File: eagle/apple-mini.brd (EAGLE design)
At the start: 127 x 73.7 mm, 41 parts, among them J1 USBMICRO, J2 JTAG, J3 RBM22DRTN, U1 FT240XS, U2 SN74LVC2G17DBV, U3 TPS2082D, U4 MCS6502, U5 MC6821, U6 AS6C62256A, U7 AT28C64B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

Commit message: Add DRC rules and logo bitmap to board layout
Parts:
- D1: device apple-mini:CHIPLED -> apple-mini:0603
- R8: value 100 -> 150
- moved C4 17.5 mm to (9.00, 58.5), turned to 180 degrees
- moved C5 17.5 mm to (26.5, 58.5), turned to 0 degrees
- moved R4 17.5 mm to (9.00, 60.5), turned to 180 degrees
- moved R5 17.5 mm to (26.5, 60.5), turned to 0 degrees
- moved R6 11.5 mm to (12.0, 59.5)
- moved R7 11.5 mm to (23.5, 59.5)
- moved C8 2.54 mm to (40.0, 49.5), turned to 180 degrees
- moved R3 0.44 mm to (12.0, 15.0)
- turned C11 to 180 degrees
- turned R10 to 180 degrees
- turned R11 to 180 degrees
- turned R12 to 180 degrees
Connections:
- net N$2: now also R6.1; no longer R7.1
- net N$3: now also R7.1; no longer R6.1
- net N$4: now also C4.1, R4.1, R6.2; no longer C5.1, R5.1, R7.2
- net N$5: now also C5.1, R5.1, R7.2; no longer C4.1, R4.1, R6.2
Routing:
- added copper zone on layer 15, net 5V
- added copper zone on layer 2, net GND
- removed copper zone on layer 2, net 5V
- removed copper zone on layer 15, net GND
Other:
- board text removed: "Apple Mini 1"
- board text removed: "REV A"
- board text removed: "St. Louis, Mo. Copyright 2015"
- board text removed: "http://github.com/sstallion/apple-mini/"

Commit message: Generate BOM
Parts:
- C4, C5: value 2.2uF -> 0.22uF
- R4, R5: value 10k -> 100k
- R8: value 150 -> 180
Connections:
- net GND: now also CLEAR.3; no longer RESET.3
- net N$2: now also CLEAR.1
- net N$3: no longer RESET.1

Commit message: Route critical signals
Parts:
- C4, C5: value 0.22uF -> 2.2uF
- R4, R5: value 100k -> 10k
- R8: value 180 -> 150
- moved R3 6.48 mm to (14.0, 8.89), flipped to the bottom, turned to 180 degrees
- moved C4 0.56 mm to (9.25, 59.0)
- moved C5 0.56 mm to (26.2, 59.0)
- moved D1 0.54 mm to (3.17, 29.8)
- moved R6 0.35 mm to (11.8, 59.8)
- moved R7 0.35 mm to (23.8, 59.8)
- moved C2 0.25 mm to (17.8, 59.8)
- moved R4 0.25 mm to (9.25, 60.5)
- moved R5 0.25 mm to (26.2, 60.5)
- moved U2 0.25 mm to (17.8, 59.8)
- moved R8 0.14 mm to (3.17, 31.2)
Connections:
- net N$3_P renamed N$1_P
- net N$4_P renamed N$2_P
- net A0: no longer U8.57
- net A1: no longer U8.59
- net A12: now also U8.33
- net A13: now also U8.34
- net A14: now also U8.35
- net A15: now also U8.36
- net A2: no longer U8.50
- net A3: no longer U8.2
- net CA1: now also U8.61; no longer U8.52
- net CA2: now also U8.62; no longer U8.56
- net CB1: now also U8.63; no longer U8.19
- net CB2: now also U8.64; no longer U8.40
- net CLEAR: now also U8.49; no longer U8.31
- net DA: now also U8.47; no longer U8.20
- net FIFO_DATA0: now also U8.1; no longer U8.43
- net FIFO_DATA1: now also U8.2; no longer U8.44
- net FIFO_DATA2: now also U8.4; no longer U8.49
- net FIFO_DATA3: now also U8.5; no longer U8.51
- net FIFO_DATA4: now also U8.6; no longer U8.8
- net FIFO_DATA5: now also U8.7; no longer U8.9
- net FIFO_DATA6: now also U8.8; no longer U8.10
- net FIFO_DATA7: now also U8.9; no longer U8.39
- net FIFO_RD: now also U8.10; no longer U8.22
- net FIFO_RXF: now also U8.12; no longer U8.48
- net FIFO_TXE: now also U8.13; no longer U8.45
- net FIFO_WR: now also U8.11; no longer U8.18
- net GND: now also RESET.3, RESET.4, U8.18, U8.27, U8.31, U8.38, U8.50; no longer U8.17, U8.23, U8.25, U8.32, U8.36
- net N$3: now also RESET.1, RESET.2
- net PA0: now also U8.51; no longer U8.6
- net PA1: now also U8.52; no longer U8.60
- net PA2: now also U8.56; no longer U8.58
- net PA3: now also U8.57; no longer U8.62
- net PA4: now also U8.58; no longer U8.63
- net PA5: now also U8.59; no longer U8.64
- net PA6: now also U8.60; no longer U8.4
- net PB0: now also U8.39; no longer U8.61
- net PB1: now also U8.40; no longer U8.5
- net PB2: now also U8.42; no longer U8.46
- net PB3: now also U8.43; no longer U8.7
- net PB4: now also U8.44; no longer U8.11
- net PB5: now also U8.45; no longer U8.13
- net PB6: now also U8.46; no longer U8.12
- net PHI0: now also U8.17; no longer U8.24
- net PHI2: now also U8.32; no longer U8.47
- net R: now also U8.19; no longer U8.27
- net RESET: now also U8.48; no longer U8.1
- net S: now also U8.20; no longer U8.33
- net T: now also U8.22; no longer U8.35
- net X: now also U8.23; no longer U8.34
- net Y: now also U8.24; no longer U8.42
- net Z: now also U8.25; no longer U8.38
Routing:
- net PHI0: track 0.00 -> 118.0 mm, vias 0 -> 1
- net TCK: track 0.00 -> 55.9 mm, vias 0 -> 2
- net GND: track 0.00 -> 27.8 mm, vias 0 -> 2
- net CLK12MHZ: track 0.00 -> 24.4 mm, vias 0 -> 2
- net N$2_N: track 0.00 -> 24.3 mm, vias 0 -> 2
- net N$2_P: track 0.00 -> 23.1 mm, vias 0 -> 2
- net 5V: track 0.00 -> 17.2 mm, vias 0 -> 4
- net N$5: track 0.00 -> 9.36 mm
- net N$4: track 0.00 -> 8.65 mm
- net N$3: track 0.00 -> 8.58 mm
- net N$2: track 0.00 -> 8.55 mm
- net N$1_N: track 0.00 -> 2.26 mm
- net N$1_P: track 0.00 -> 2.26 mm
- net 5V_IN: track 0.00 -> 1.80 mm, vias 0 -> 1
- net N$1: track 0.00 -> 1.50 mm
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- added copper zone on layer 1, net N$6

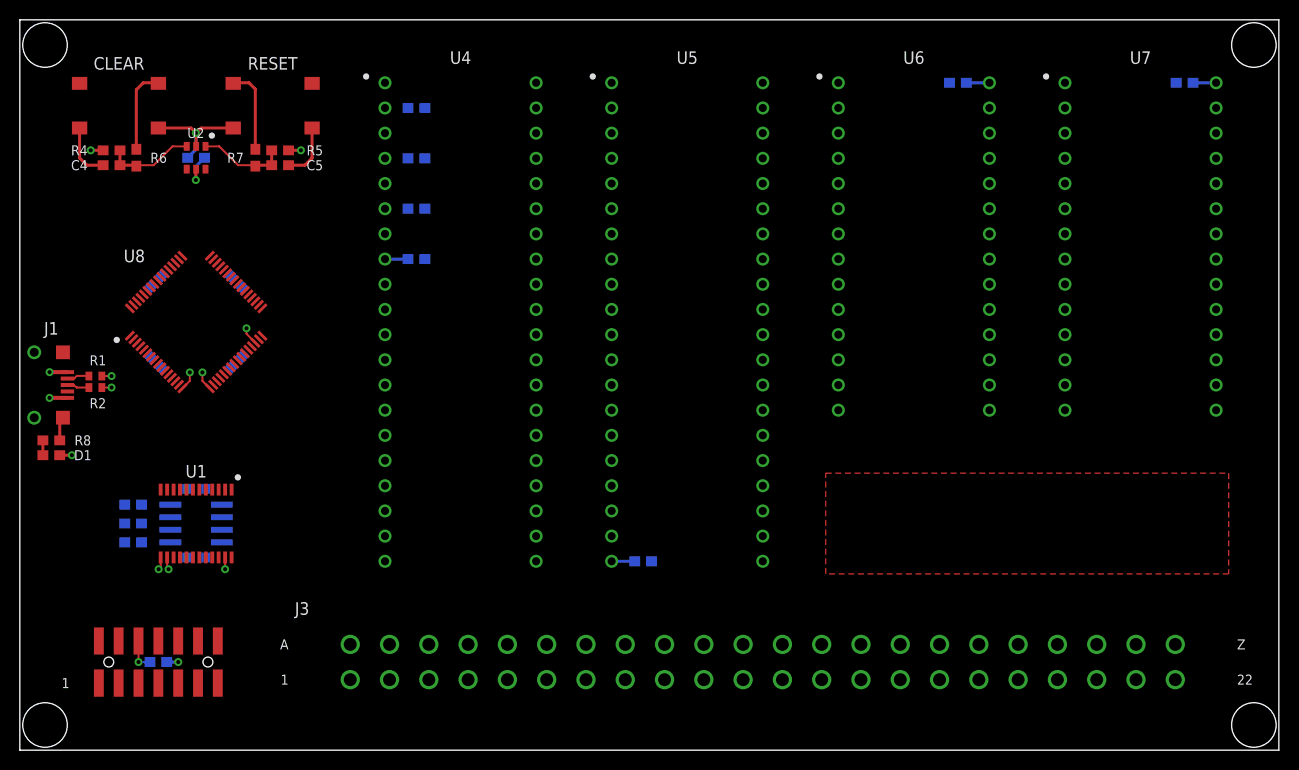
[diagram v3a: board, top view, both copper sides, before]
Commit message: Route power and remaining critical nets
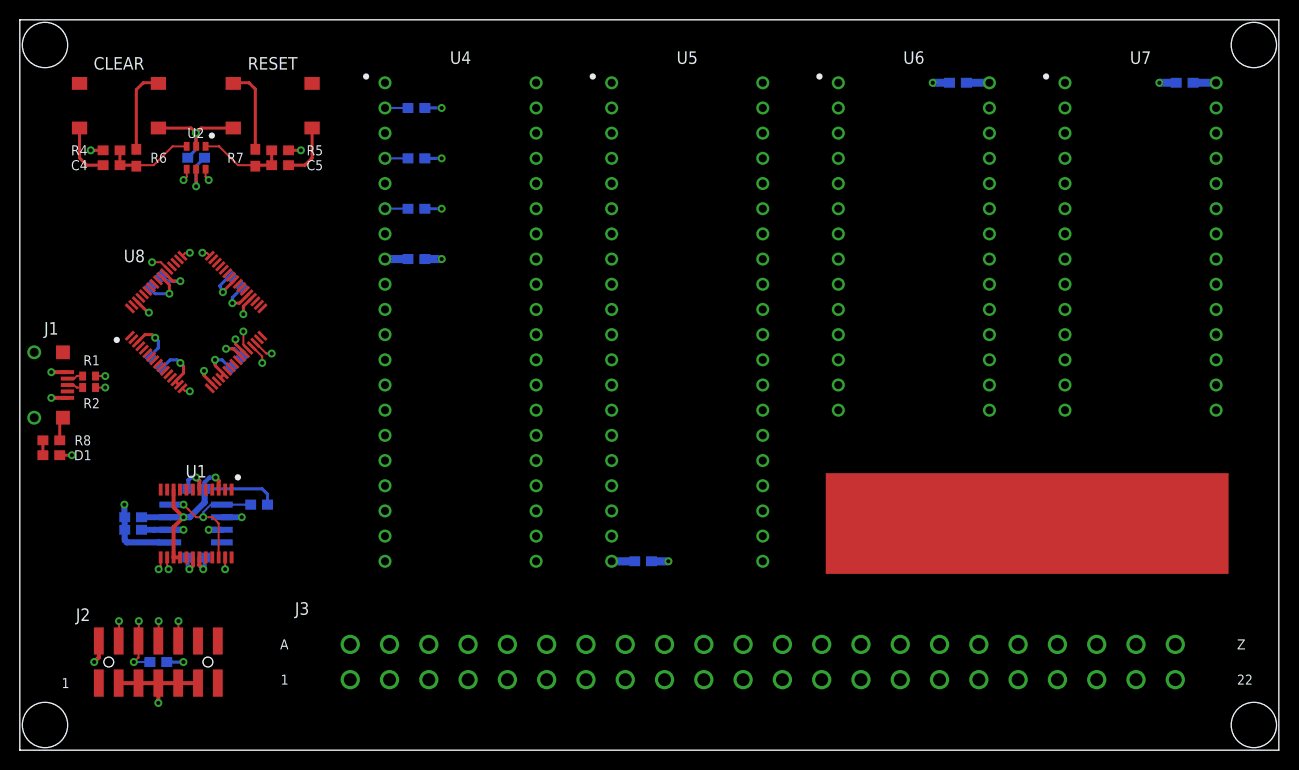
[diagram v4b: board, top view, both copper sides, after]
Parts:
- moved R9 12.7 mm to (24.1, 24.8), turned to 180 degrees
- moved C6 1.27 mm to (11.4, 22.2)
- moved C7 0.64 mm to (11.4, 23.5)
- moved R1 0.63 mm to (6.99, 37.7)
- moved R2 0.63 mm to (6.99, 36.6)
- turned C13 to 135 degrees
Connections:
- net A15: now also U8.38; no longer U8.36
- net CA1: now also U8.51; no longer U8.61
- net CA2: now also U8.56; no longer U8.62
- net DA: now also U8.39; no longer U8.47
- net FIFO_DATA0: now also U8.13; no longer U8.1
- net FIFO_DATA1: now also U8.9; no longer U8.2
- net FIFO_DATA2: now also U8.11; no longer U8.4
- net FIFO_DATA3: now also U8.4; no longer U8.5
- net FIFO_DATA4: now also U8.12; no longer U8.6
- net FIFO_DATA5: now also U8.6; no longer U8.7
- net FIFO_DATA6: now also U8.5; no longer U8.8
- net FIFO_DATA7: now also U8.7; no longer U8.9
- net FIFO_RD: now also U8.2; no longer U8.10
- net FIFO_RXF: now also U8.10; no longer U8.12
- net FIFO_TXE: now also U8.8; no longer U8.13
- net FIFO_WR: now also U8.1; no longer U8.11
- net GND: now also U8.20, U8.36, U8.62; no longer U8.31, U8.38, U8.50
- net PA0: now also U8.50; no longer U8.51
- net PA2: now also U8.57; no longer U8.56
- net PA3: now also U8.59; no longer U8.57
- net PA5: now also U8.60; no longer U8.59
- net PA6: now also U8.61; no longer U8.60
- net PB0: now also U8.47; no longer U8.39
- net PB1: now also U8.46; no longer U8.40
- net PB2: now also U8.45; no longer U8.42
- net PB3: now also U8.44; no longer U8.43
- net PB4: now also U8.43; no longer U8.44
- net PB5: now also U8.42; no longer U8.45
- net PB6: now also U8.40; no longer U8.46
- net PHI2: now also U8.19; no longer U8.32
- net R: now also U8.23; no longer U8.19
- net S: now also U8.22; no longer U8.20
- net T: now also U8.31; no longer U8.22
- net X: now also U8.32; no longer U8.23
- net Y: now also U8.25; no longer U8.24
- net Z: now also U8.24; no longer U8.25
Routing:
- net PHI0: track 118.0 -> 0.00 mm, vias 1 -> 0
- net GND: track 27.8 -> 83.6 mm, vias 2 -> 18
- net TDO: track 0.00 -> 51.2 mm, vias 0 -> 2
- net TDI: track 0.00 -> 43.9 mm, vias 0 -> 2
- net TMS: track 0.00 -> 41.7 mm, vias 0 -> 2
- net 3V3_IN: track 0.00 -> 28.5 mm, vias 0 -> 2
- net 3V3: track 1.16 -> 22.9 mm, vias 1 -> 7
- net PWREN: track 0.00 -> 14.7 mm, vias 0 -> 2
- net TCK: track 55.9 -> 45.7 mm, vias 2 -> 3
- net CLEAR: track 0.00 -> 9.69 mm, vias 0 -> 2
- net RESET: track 0.00 -> 9.69 mm, vias 0 -> 2
- net 5V: track 17.2 -> 25.1 mm, vias 4 -> 8
- net 5V_IN: track 1.80 -> 8.95 mm, vias 1 -> 3
- net CLK12MHZ: track 24.4 -> 21.5 mm
- net RDY: track 0.00 -> 2.33 mm
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- added copper zone on layer 15, net 3V3
- added copper zone on layer 15, net 5V_IN
- added copper zone on layer 15, net N$6
- removed copper zone on layer 1, net N$6
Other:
- board text removed: "#8-32 Loose Fit"

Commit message: Initial (and incomplete) gerbers
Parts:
- moved R9 12.1 mm to (12.1, 24.8), turned to 0 degrees
- moved D1 0.71 mm to (2.54, 30.1)
- moved R8 0.71 mm to (2.54, 31.6)
- moved C6 0.63 mm to (12.1, 22.2)
- moved C7 0.63 mm to (12.1, 23.5)
- moved C10 0.32 mm to (117.8, 67.3)
- moved C9 0.32 mm to (94.9, 67.3)
- moved C11 0.32 mm to (62.5, 19.1)
- moved C8 0.32 mm to (39.7, 49.5)
- moved R10 0.32 mm to (39.7, 64.8)
- moved R11 0.32 mm to (39.7, 59.7)
- moved R12 0.32 mm to (39.7, 54.6)
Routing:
- net 5V_IN: track 8.95 -> 39.8 mm
- net TDO: track 51.2 -> 61.1 mm
- net GND: track 83.6 -> 78.0 mm, vias 18 -> 20
- net 5V: track 25.1 -> 22.9 mm
- net PWREN: track 14.7 -> 13.2 mm
- net 3V3: track 22.9 -> 21.6 mm
- net TDI: track 43.9 -> 43.0 mm
- net TCK: track 45.7 -> 45.0 mm
- net 3V3_IN: vias 2 -> 3
- removed copper zone on layer 15, net 5V_IN
- removed copper zone on layer 15, net N$6
